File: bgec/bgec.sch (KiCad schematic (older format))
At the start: 5 parts

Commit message: Add clock
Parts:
- added C1: 100nF, symbol Device:C
- added CLK16MHz: DSC6001CI2A-016.0000T, 4-LEAD_CDFN-3.2X2.5_1, symbol bgec:DSC6001CI2A-016.0000T
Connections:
- net GCLogic renamed +3V3
- net +3V3: now also C1.1, CLK16MHz.1 (OE), CLK16MHz.4 (VDD)
- new net: C1.2, CLK16MHz.2 (GND)
- new net CLK: CLK16MHz.3 (OUT)
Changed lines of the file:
@@
 	1    0    0    -1
 $EndComp
-Text GLabel 6000 1000 0    50   Input ~ 0
+Text GLabel 5500 1000 0    50   Input ~ 0
 GCLogic
-Text GLabel 6000 1100 0    50   Input ~ 0
+Text GLabel 5500 1100 0    50   Input ~ 0
 GCRumble
-Text GLabel 6000 1200 0    50   Input ~ 0
+Text GLabel 5500 1200 0    50   Input ~ 0
 GCData
-Text GLabel 6000 1300 0    50   Input ~ 0
+Text GLabel 5500 1300 0    50   Input ~ 0
 GCLogicGround
-Text GLabel 6000 1400 0    50   Input ~ 0
+Text GLabel 5500 1400 0    50   Input ~ 0
 GCRumbleGround
 $Comp
@@
 	3900 1100 3900 1200
 Connection ~ 3800 1100
+$Comp
+L bgec:DSC6001CI2A-016.0000T CLK16MHz
+U 1 1 5E554F81
+P 7500 1000
+F 0 "CLK16MHz" H 7900 1450 50  0000 C CNN
+F 1 "DSC6001CI2A-016.0000T" H 7900 1350 50  0000 C CNN
+F 2 "4-LEAD_CDFN-3.2X2.5_1" H 8600 2500 50  0001 L CNN
+F 3 "https://componentsearchengine.com/Datasheets/1/DSC6001CI2A-016.0000T.pdf" H 8600 2400 50  0001 L CNN
+F 4 "Standard Clock Oscillators MEMS Oscillator, Ultra Low Power, LVCMOS, -40C-85C, 25ppm, 3.2x2.5mm" H 8600 2300 50  0001 L CNN "Description"
+F 5 "" H 8150 800 50  0001 L CNN "Height"
+F 6 "579-6001CI2A0160000T" H 8600 2100 50  0001 L CNN "Mouser Part Number"
+F 7 "https://www.mouser.com/Search/Refine.aspx?Keyword=579-6001CI2A0160000T" H 8600 2000 50  0001 L CNN "Mouser Price/Stock"
+F 8 "Microchip" H 8600 1900 50  0001 L CNN "Manufacturer_Name"
+F 9 "DSC6001CI2A-016.0000T" H 8600 1800 50  0001 L CNN "Manufacturer_Part_Number"
+	1    7500 1000
+	1    0    0    -1
+$EndComp
+Text GLabel 8500 1100 2    50   Input ~ 0
+CLK
+Wire Wire Line
+	8300 1100 8500 1100
+Text GLabel 7000 800  0    50   Input ~ 0
+GCLogic
+Wire Wire Line
+	8300 800  8300 1000
+Wire Wire Line
+	7500 1000 7500 800
+Connection ~ 7500 800
+Wire Wire Line
+	7500 800  8300 800
+Wire Wire Line
+	5500 1000 5600 1000
+$Comp
+L power:+3V3 #PWR?
+U 1 1 5E562812
+P 5600 1000
+F 0 "#PWR?" H 5600 850 50  0001 C CNN
+F 1 "+3V3" V 5615 1128 50  0000 L CNN
+F 2 "" H 5600 1000 50  0001 C CNN
+F 3 "" H 5600 1000 50  0001 C CNN
+	1    5600 1000
+	0    1    1    0
+$EndComp
+Wire Wire Line
+	5500 1100 5600 1100
+$Comp
+L power:+5V #PWR?
+U 1 1 5E564ED9
+P 5600 1100
+F 0 "#PWR?" H 5600 950 50  0001 C CNN
+F 1 "+5V" V 5615 1228 50  0000 L CNN
+F 2 "" H 5600 1100 50  0001 C CNN
+F 3 "" H 5600 1100 50  0001 C CNN
+	1    5600 1100
+	0    1    1    0
+$EndComp
+$Comp
+L Device:C C1
+U 1 1 5E566884
+P 7250 1100
+F 0 "C1" V 7502 1100 50  0000 C CNN
+F 1 "100nF" V 7411 1100 50  0000 C CNN
+F 2 "" H 7288 950 50  0001 C CNN
+F 3 "~" H 7250 1100 50  0001 C CNN
+	1    7250 1100
+	0    -1   -1   0
+$EndComp
+Wire Wire Line
+	7000 800  7100 800
+Wire Wire Line
+	7100 800  7100 1100
+Connection ~ 7100 800
+Wire Wire Line
+	7100 800  7500 800
+Wire Wire Line
+	7400 1100 7500 1100
+Wire Wire Line
+	5500 1300 5600 1300
+$Comp
+L power:GND #PWR?
+U 1 1 5E570CAB
+P 5600 1300
+F 0 "#PWR?" H 5600 1050 50  0001 C CNN
+F 1 "GND" V 5605 1172 50  0000 R CNN
+F 2 "" H 5600 1300 50  0001 C CNN
+F 3 "" H 5600 1300 50  0001 C CNN
+	1    5600 1300
+	0    -1   -1   0
+$EndComp
+$Comp
+L power:GND #PWR?
+U 1 1 5E5721CB
+P 5600 1400
+F 0 "#PWR?" H 5600 1150 50  0001 C CNN
+F 1 "GND" V 5605 1272 50  0000 R CNN
+F 2 "" H 5600 1400 50  0001 C CNN
+F 3 "" H 5600 1400 50  0001 C CNN
+	1    5600 1400
+	0    -1   -1   0
+$EndComp
+Wire Wire Line
+	5500 1400 5600 1400
 $EndSCHEMATC

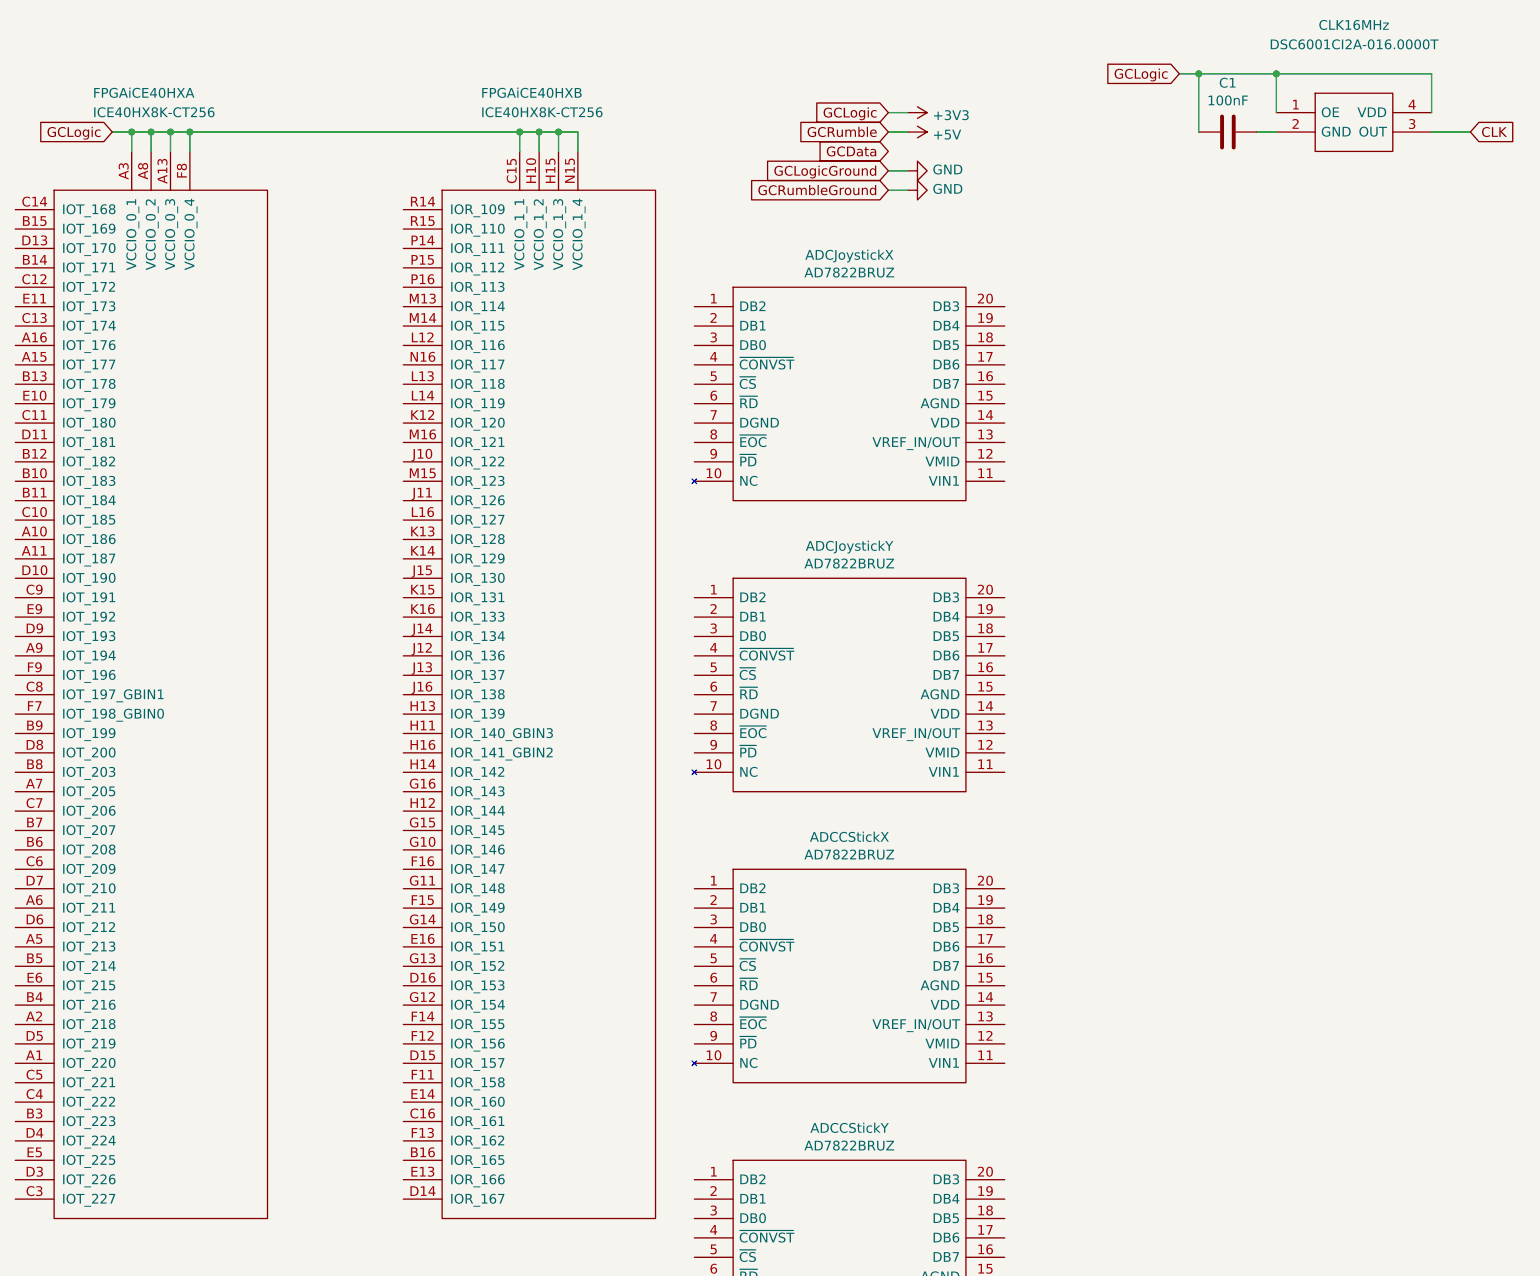
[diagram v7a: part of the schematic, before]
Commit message: Annotate items so PCB can be generated
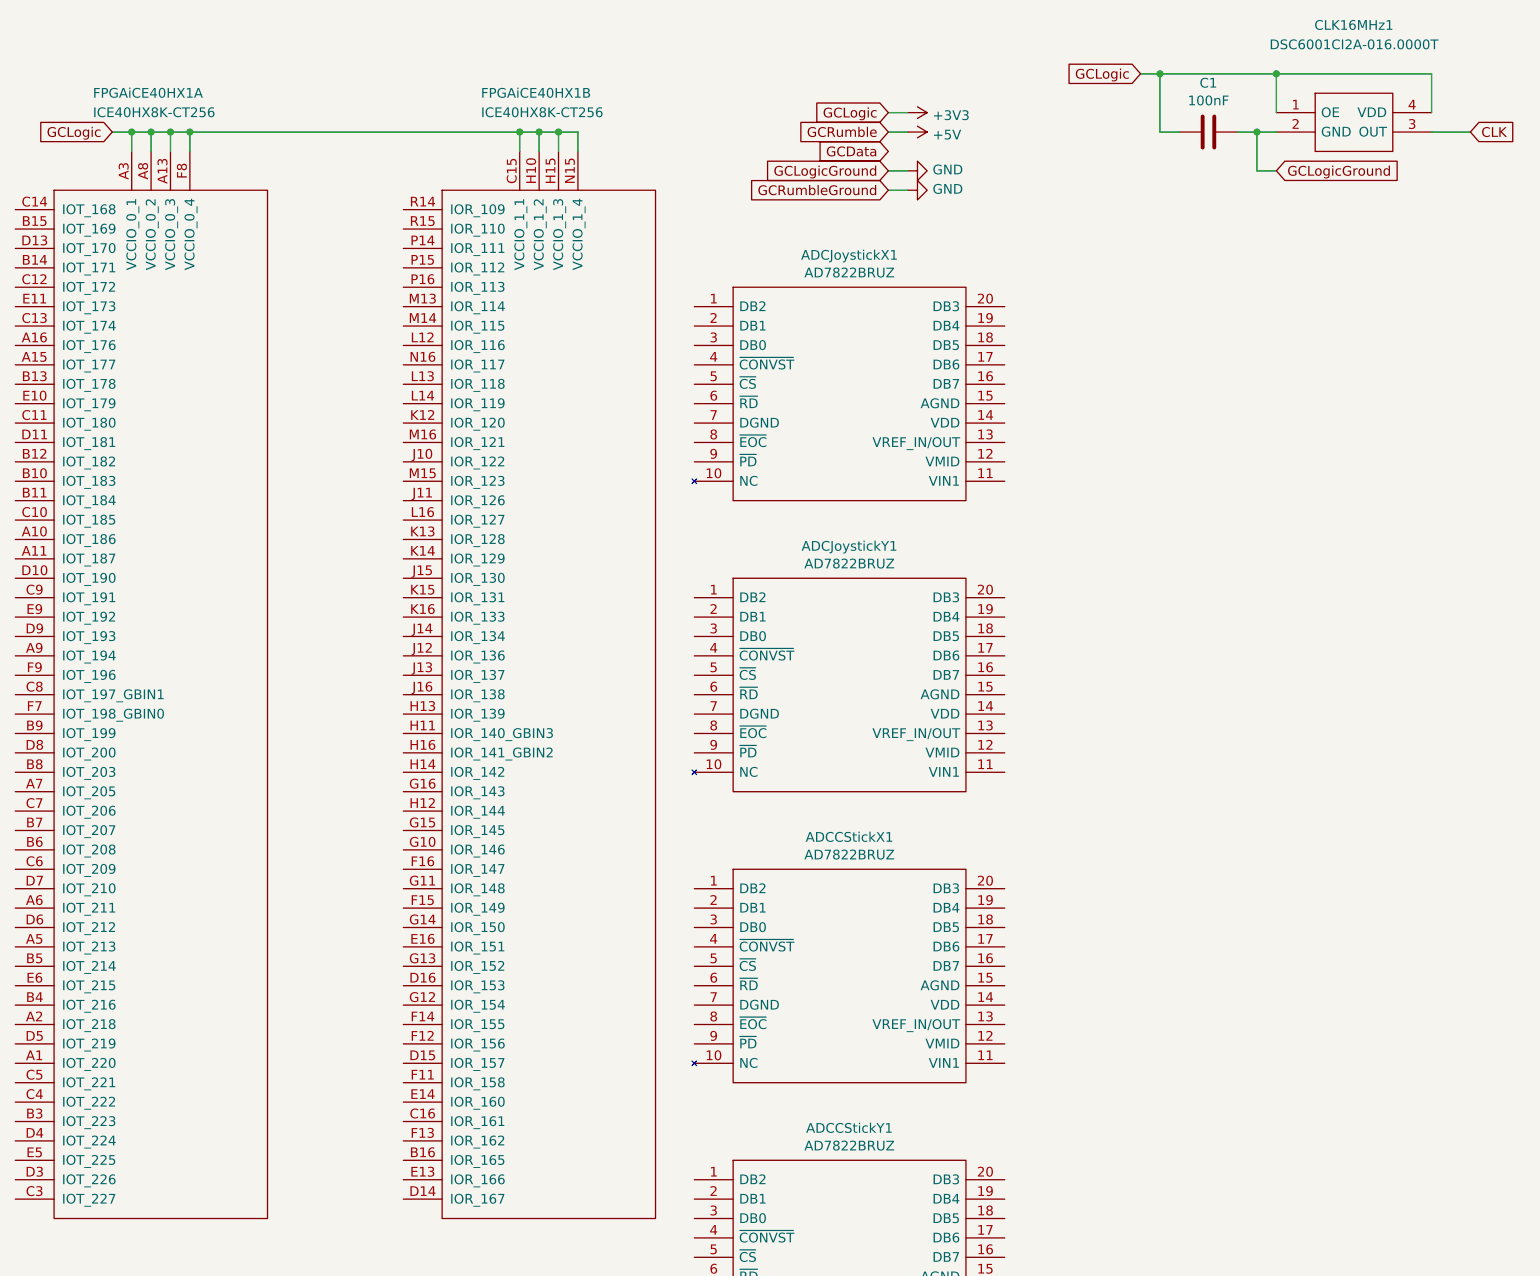
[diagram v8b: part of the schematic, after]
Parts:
- renumbered ADCCStickX to ADCCStickX1, ADCCStickY to ADCCStickY1, ADCJoystickX to ADCJoystickX1, ADCJoystickY to ADCJoystickY1, CLK16MHz to CLK16MHz1, FPGAiCE40HX to FPGAiCE40HX1
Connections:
- net GND: now also C1.2, CLK16MHz1.2 (GND)
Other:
- moved on the sheet: C1
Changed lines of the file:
@@
 $EndDescr
 $Comp
-L bgec:AD7822BRUZ ADCJoystickX
+L bgec:AD7822BRUZ ADCJoystickX1
 U 1 1 5E4E3FD4
 P 4500 2000
-F 0 "ADCJoystickX" H 5300 2265 50  0000 C CNN
+F 0 "ADCJoystickX1" H 5300 2265 50  0000 C CNN
 F 1 "AD7822BRUZ" H 5300 2174 50  0000 C CNN
 F 2 "SOP65P640X120-20N" H 5950 2100 50  0001 L CNN
@@
 $EndComp
 $Comp
-L bgec:AD7822BRUZ ADCJoystickY
+L bgec:AD7822BRUZ ADCJoystickY1
 U 1 1 5E4E4DBF
 P 4500 3500
-F 0 "ADCJoystickY" H 5300 3765 50  0000 C CNN
+F 0 "ADCJoystickY1" H 5300 3765 50  0000 C CNN
 F 1 "AD7822BRUZ" H 5300 3674 50  0000 C CNN
 F 2 "SOP65P640X120-20N" H 5950 3600 50  0001 L CNN
@@
 $EndComp
 $Comp
-L bgec:AD7822BRUZ ADCCStickX
+L bgec:AD7822BRUZ ADCCStickX1
 U 1 1 5E4E5FF1
 P 4500 5000
-F 0 "ADCCStickX" H 5300 5265 50  0000 C CNN
+F 0 "ADCCStickX1" H 5300 5265 50  0000 C CNN
 F 1 "AD7822BRUZ" H 5300 5174 50  0000 C CNN
 F 2 "SOP65P640X120-20N" H 5950 5100 50  0001 L CNN
@@
 $EndComp
 $Comp
-L bgec:AD7822BRUZ ADCCStickY
+L bgec:AD7822BRUZ ADCCStickY1
 U 1 1 5E4E6A54
 P 4500 6500
-F 0 "ADCCStickY" H 5300 6765 50  0000 C CNN
+F 0 "ADCCStickY1" H 5300 6765 50  0000 C CNN
 F 1 "AD7822BRUZ" H 5300 6674 50  0000 C CNN
 F 2 "SOP65P640X120-20N" H 5950 6600 50  0001 L CNN
@@
 GCRumbleGround
 $Comp
-L bgec:ICE40HX8K-CT256 FPGAiCE40HX
+L bgec:ICE40HX8K-CT256 FPGAiCE40HX1
 U 1 1 5E50B913
 P 1000 1500
-F 0 "FPGAiCE40HX" H 1400 2100 50  0000 L CNN
+F 0 "FPGAiCE40HX1" H 1400 2100 50  0000 L CNN
 F 1 "ICE40HX8K-CT256" H 1400 2000 50  0000 L CNN
 F 2 "bgec:BGA256C80P16X16_1400X1400X170" H 1750 2250 50  0001 C CNN
@@
 Connection ~ 1800 1100
 $Comp
-L bgec:ICE40HX8K-CT256 FPGAiCE40HX
+L bgec:ICE40HX8K-CT256 FPGAiCE40HX1
 U 2 1 5E506C35
 P 3000 1500
-F 0 "FPGAiCE40HX" H 3400 2100 50  0000 L CNN
+F 0 "FPGAiCE40HX1" H 3400 2100 50  0000 L CNN
 F 1 "ICE40HX8K-CT256" H 3400 2000 50  0000 L CNN
 F 2 "bgec:BGA256C80P16X16_1400X1400X170" H 4250 2500 50  0001 C CNN
@@
 Connection ~ 3800 1100
 $Comp
-L bgec:DSC6001CI2A-016.0000T CLK16MHz
+L bgec:DSC6001CI2A-016.0000T CLK16MHz1
 U 1 1 5E554F81
 P 7500 1000
-F 0 "CLK16MHz" H 7900 1450 50  0000 C CNN
+F 0 "CLK16MHz1" H 7900 1450 50  0000 C CNN
 F 1 "DSC6001CI2A-016.0000T" H 7900 1350 50  0000 C CNN
 F 2 "4-LEAD_CDFN-3.2X2.5_1" H 8600 2500 50  0001 L CNN
@@
 Wire Wire Line
 	8300 1100 8500 1100
-Text GLabel 7000 800  0    50   Input ~ 0
+Text GLabel 6800 800  0    50   Input ~ 0
 GCLogic
 Wire Wire Line
@@
 	5500 1000 5600 1000
 $Comp
-L power:+3V3 #PWR?
+L power:+3V3 #PWR0101
 U 1 1 5E562812
 P 5600 1000
-F 0 "#PWR?" H 5600 850 50  0001 C CNN
+F 0 "#PWR0101" H 5600 850 50  0001 C CNN
 F 1 "+3V3" V 5615 1128 50  0000 L CNN
 F 2 "" H 5600 1000 50  0001 C CNN
@@
 	5500 1100 5600 1100
 $Comp
-L power:+5V #PWR?
+L power:+5V #PWR0102
 U 1 1 5E564ED9
 P 5600 1100
-F 0 "#PWR?" H 5600 950 50  0001 C CNN
+F 0 "#PWR0102" H 5600 950 50  0001 C CNN
 F 1 "+5V" V 5615 1228 50  0000 L CNN
 F 2 "" H 5600 1100 50  0001 C CNN
@@
 L Device:C C1
 U 1 1 5E566884
-P 7250 1100
-F 0 "C1" V 7502 1100 50  0000 C CNN
-F 1 "100nF" V 7411 1100 50  0000 C CNN
-F 2 "" H 7288 950 50  0001 C CNN
-F 3 "~" H 7250 1100 50  0001 C CNN
-	1    7250 1100
+P 7150 1100
+F 0 "C1" V 7402 1100 50  0000 C CNN
+F 1 "100nF" V 7311 1100 50  0000 C CNN
+F 2 "" H 7188 950 50  0001 C CNN
+F 3 "~" H 7150 1100 50  0001 C CNN
+	1    7150 1100
 	0    -1   -1   0
 $EndComp
 Wire Wire Line
-	7000 800  7100 800
-Wire Wire Line
-	7100 800  7100 1100
-Connection ~ 7100 800
-Wire Wire Line
-	7100 800  7500 800
-Wire Wire Line
-	7400 1100 7500 1100
+	6900 800  6900 1100
 Wire Wire Line
 	5500 1300 5600 1300
 $Comp
-L power:GND #PWR?
+L power:GND #PWR0103
 U 1 1 5E570CAB
 P 5600 1300
-F 0 "#PWR?" H 5600 1050 50  0001 C CNN
+F 0 "#PWR0103" H 5600 1050 50  0001 C CNN
 F 1 "GND" V 5605 1172 50  0000 R CNN
 F 2 "" H 5600 1300 50  0001 C CNN
@@
 $EndComp
 $Comp
-L power:GND #PWR?
+L power:GND #PWR0104
 U 1 1 5E5721CB
 P 5600 1400
-F 0 "#PWR?" H 5600 1150 50  0001 C CNN
+F 0 "#PWR0104" H 5600 1150 50  0001 C CNN
 F 1 "GND" V 5605 1272 50  0000 R CNN
 F 2 "" H 5600 1400 50  0001 C CNN
@@
 Wire Wire Line
 	5500 1400 5600 1400
+Wire Wire Line
+	6800 800  6900 800
+Connection ~ 6900 800
+Wire Wire Line
+	6900 800  7500 800
+Wire Wire Line
+	6900 1100 7000 1100
+Wire Wire Line
+	7300 1100 7400 1100
+Wire Wire Line
+	7400 1100 7400 1300
+Wire Wire Line
+	7400 1300 7500 1300
+Connection ~ 7400 1100
+Wire Wire Line
+	7400 1100 7500 1100
+Text GLabel 7500 1300 2    50   Input ~ 0
+GCLogicGround
 $EndSCHEMATC
